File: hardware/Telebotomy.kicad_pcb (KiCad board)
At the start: 2 copper layers, 88 x 20.7 mm, 23 parts, among them J1 10118193-0001LF, J2 RJHSE-5080, J3 Conn_02x03_Odd_Even, J4 Conn_02x03_Odd_Even, J5 RJHSE-5080, J6 Conn_01x06_Pin, J7 Conn_01x04_Pin, U1 KSZ8863MLL, U2 ATTINY85-20PU, U3 MIC5504-3.3YM5_TR

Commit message: PCB Updates
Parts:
- added G***: LOGO, telebotomy:arrow, F.Cu at (128.0, 114.5)
- added G***: LOGO, telebotomy:arrow, F.Cu at (166.4, 114.3)
- added G***: LOGO, telebotomy:lamemakes_logo, B.Cu at (162.1, 78.9)
- added TP1: TestPoint, TestPoint:TestPoint_Pad_D1.0mm, F.Cu at (127.3, 78.2)
- added TP2: TestPoint, TestPoint:TestPoint_Pad_D1.0mm, F.Cu at (127.3, 81.0)
- moved J2 53.1 mm to (137.4, 110.4), turned to 0 degrees
- moved J5 49.4 mm to (157.0, 110.4), turned to 0 degrees
- moved R9 36.1 mm to (157.0, 82.5)
- moved R3 36.0 mm to (152.0, 78.2), turned to 0 degrees
- moved R4 28.7 mm to (145.3, 78.2), turned to 0 degrees
- moved J3 23.2 mm to (151.8, 85.9), turned to 180 degrees
- moved U3 21.2 mm to (158.1, 90.2), turned to 180 degrees
- moved D4 20.1 mm to (158.1, 93.3), turned to 0 degrees
- moved R7 19.2 mm to (160.9, 82.5), turned to -90 degrees
- moved J4 18.9 mm to (145.1, 85.9), turned to 180 degrees
- moved R8 17.3 mm to (158.3, 95.4)
- moved R6 16.9 mm to (164.9, 82.5), turned to -90 degrees
- moved J6 15.4 mm to (137.8, 95.8), turned to 180 degrees
- moved R2 12.4 mm to (135.0, 95.9)
- moved J7 9.55 mm to (137.8, 79.2)
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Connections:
- J2 pad 1: /TXP2 -> /TX1_P
- J2 pad 2: /TXM2 -> /TX1_N
- J2 pad 3: /RXP2 -> /RX1_P
- J2 pad 6: /RXM2 -> /RX1_N
- J5 pad 1: /TXP1 -> /TX2_P
- J5 pad 2: /TXM1 -> /TX2_N
- J5 pad 3: /RXP1 -> /RX2_P
- J5 pad 6: /RXM1 -> /RX2_N
- U1 pad 1: /RXM1 -> /RX1_N
- U1 pad 11: /TXM1 -> /TX2_N
- U1 pad 12: /TXP2 -> /TX2_P
- U1 pad 2: /RXP1 -> /RX1_P
- U1 pad 3: /TXM1 -> /TX1_N
- U1 pad 4: /TXP1 -> /TX1_P
- U1 pad 8: /RXM2 -> /RX2_N
- U1 pad 9: /RXP1 -> /RX2_P
- U2 pad 2: /REM_IN1 -> /REM_IN2
- U2 pad 3: /REM_IN2 -> /REM_IN1
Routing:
- net /+3v3: track 0.00 -> 58.1 mm, vias 0 -> 7
- net /AT_PWR: track 0.00 -> 34.9 mm, vias 0 -> 3
- net /AT_LED: track 0.00 -> 29.1 mm, vias 0 -> 1
- net /P1LED1: track 0.00 -> 28.8 mm, vias 0 -> 2
- net /REM_IN1: track 0.00 -> 27.6 mm, vias 0 -> 4
- net /P1LED0: track 0.00 -> 22.2 mm, vias 0 -> 1
- net /LINK_LED: track 0.00 -> 20.2 mm, vias 0 -> 1
- net /SCL: track 0.00 -> 19.9 mm, vias 0 -> 2
- net /ACT_LED: track 0.00 -> 19.3 mm, vias 0 -> 1
- net /TX2_P: track 0.00 -> 17.2 mm
- net /RX2_P: track 0.00 -> 16.6 mm
- net /REM_IN2: track 0.00 -> 15.8 mm, vias 0 -> 3
- net /TX2_N: track 0.00 -> 15.7 mm
- net Net-(J1-SHIELD-PadS1): track 0.00 -> 14.3 mm
- net /SDA: track 0.00 -> 13.8 mm, vias 0 -> 2
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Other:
- board size 88 x 20.7 mm -> 43.3 x 40.4 mm
- board text added: "3v3"
- board text added: "ACT"
- board text added: "GND"
- board text added: "LNK"
- board text added: "Net In"
- board text added: "PWR"
- board text added: "RE1"
- board text added: "RE2"
- board text added: "TV Out"

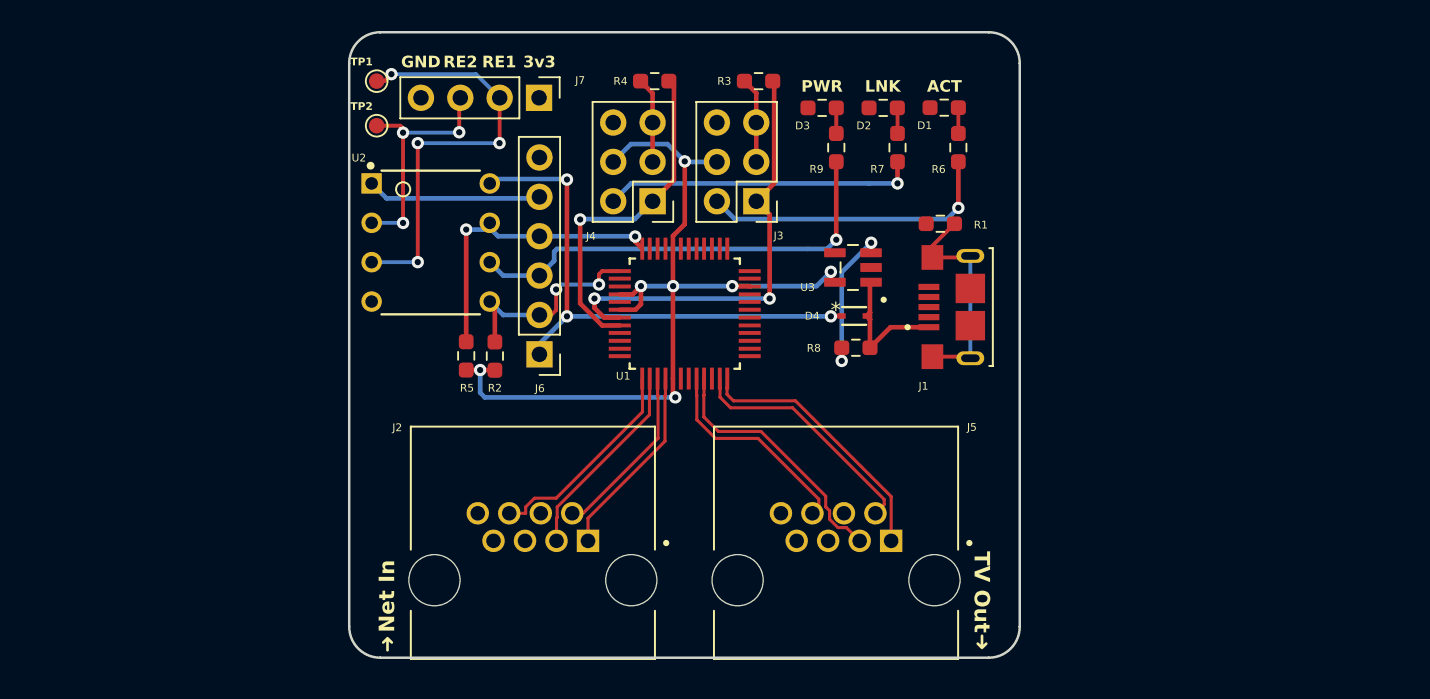
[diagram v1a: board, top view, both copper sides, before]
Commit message: Closer to final PCB, updated CI to include snip of PCB
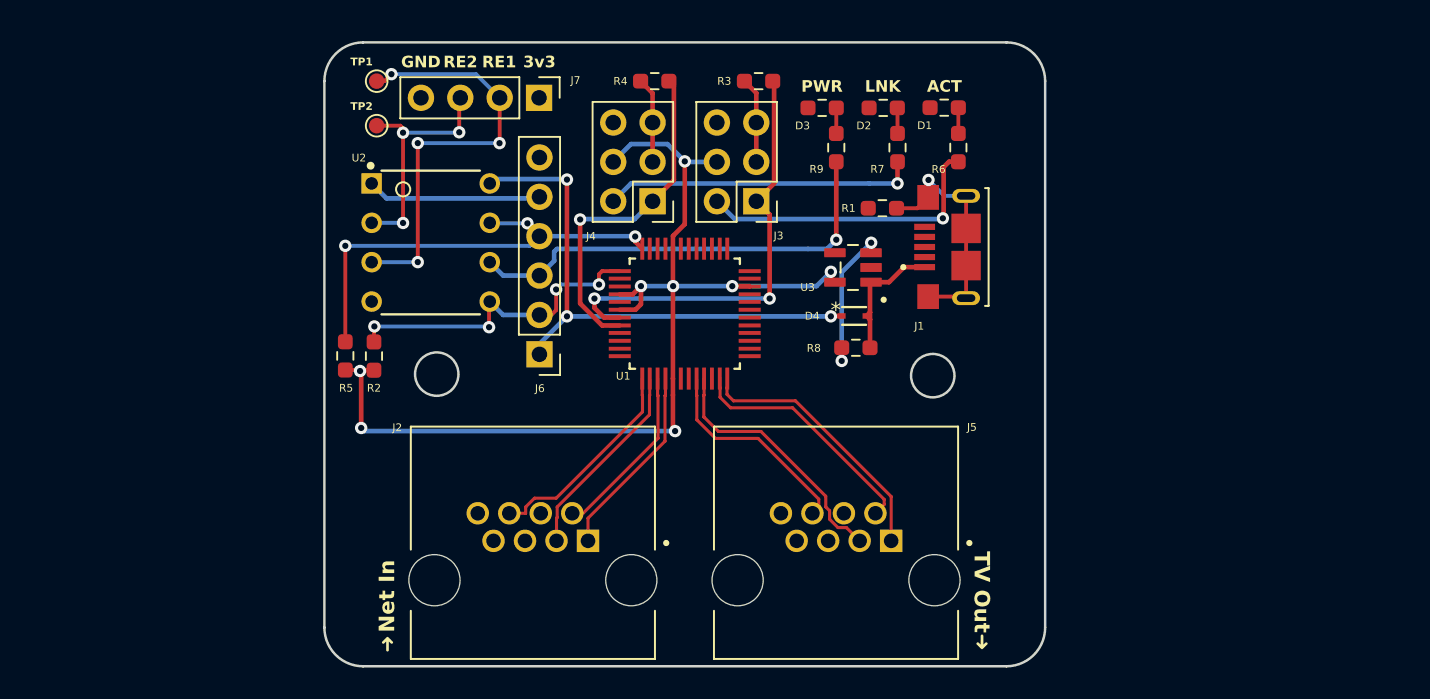
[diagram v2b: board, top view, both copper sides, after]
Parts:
- moved R5 7.80 mm to (125.3, 95.9)
- moved R2 7.80 mm to (127.2, 95.9)
- moved J1 3.88 mm to (165.4, 88.9)
- moved R1 3.87 mm to (160.0, 86.4)
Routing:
- net /+3v3: track 58.1 -> 70.2 mm, vias 7 -> 8
- net /SCL: track 19.9 -> 30.1 mm, vias 2 -> 3
- net /SDA: track 13.8 -> 21.7 mm, vias 2 -> 4
- net Net-(J1-SHIELD-PadS1): track 14.3 -> 15.4 mm, vias 0 -> 1
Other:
- board size 43.3 x 40.4 mm -> 46.5 x 40.2 mm
- board text added: "MK I"
- board text added: "Telebotomy"

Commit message: PCB updates
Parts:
- added REF**: MountingHole_2.7mm_M2.5_DIN965_Pad, MountingHole:MountingHole_2.7mm_M2.5_DIN965_Pad, F.Cu at (163.2, 97.2)
- added REF**: MountingHole_2.7mm_M2.5_DIN965_Pad, MountingHole:MountingHole_2.7mm_M2.5_DIN965_Pad, F.Cu at (131.2, 97.1)
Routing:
- net GND: track 0.00 -> 24.0 mm, vias 0 -> 12
- net /+3v3: track 70.2 -> 82.9 mm
- net /RX2_P: track 16.6 -> 12.6 mm
- added copper zone on B.Cu, net GND
- added copper zone on F.Cu, net GND
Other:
- outline, holes or cut-outs redrawn
